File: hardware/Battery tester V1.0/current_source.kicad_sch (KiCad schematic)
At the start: 13 parts, among them K1 Relay_DPDT, Q1 IRF540N, U1 LM358

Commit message: update man pcb, cleanup
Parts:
- added C4: 100n, Capacitor_SMD:C_0805_2012Metric_Pad1.18x1.45mm_HandSolder, symbol Device:C
- added D1: 1N4148, Diode_THT:D_DO-35_SOD27_P7.62mm_Horizontal, symbol Diode:1N4148
- added Q2: BC817, Package_TO_SOT_SMD:SOT-23, symbol Transistor_BJT:BC817
- added R12: 10k, symbol Device:R
- C1: value C -> 100n; footprint (none) -> Capacitor_SMD:C_0805_2012Metric_Pad1.18x1.45mm_HandSolder
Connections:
- net GND: now reaches C3.2, R9.1
- net GND: now also C1.2, C4.2, Q2.2 (E)
- net -5V: now reaches U1.4 (V-)
- net -5V: now also C4.1
- net +5V: now reaches C1.1, U1.8 (V+)
- net +12V: now reaches K1.A1
- net +12V: now also D1.1 (K)
- net at K1.A2: now also D1.2 (A), Q2.3 (C)
- new net: Q2.1 (B), R12.1
- new net SWITCH_RANGE: R12.2

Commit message: update main pcb schematic
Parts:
- C10: renamed from C2; footprint (none) -> Capacitor_SMD:C_0805_2012Metric_Pad1.18x1.45mm_HandSolder
- C9: renamed from C3; footprint (none) -> Capacitor_SMD:C_0805_2012Metric_Pad1.18x1.45mm_HandSolder
- R10: renamed from R6; footprint (none) -> Capacitor_SMD:C_0805_2012Metric_Pad1.18x1.45mm_HandSolder
- R11: renamed from R3; footprint (none) -> Capacitor_SMD:C_0805_2012Metric_Pad1.18x1.45mm_HandSolder
- R12: renamed from R4; footprint (none) -> Capacitor_SMD:C_0805_2012Metric_Pad1.18x1.45mm_HandSolder
- R5: renamed from R8; footprint (none) -> Capacitor_SMD:C_0805_2012Metric_Pad1.18x1.45mm_HandSolder
- R6: renamed from R9; footprint (none) -> Capacitor_SMD:C_0805_2012Metric_Pad1.18x1.45mm_HandSolder
- R7: footprint (none) -> Capacitor_SMD:C_0805_2012Metric_Pad1.18x1.45mm_HandSolder
- R8: renamed from R12; footprint (none) -> Capacitor_SMD:C_0805_2012Metric_Pad1.18x1.45mm_HandSolder
- R9: renamed from R5; footprint (none) -> Capacitor_SMD:C_0805_2012Metric_Pad1.18x1.45mm_HandSolder
- U2: renamed from U1; footprint (none) -> Package_SO:SO-8_3.9x4.9mm_P1.27mm
- renumbered C1 to C7, C4 to C8, Q2 to Q1, Q1 to Q2
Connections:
- net DAC_CURRENT: now reaches U2.3 (+)
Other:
- note added: "DISCHARGE CURRENT FEEDBACK"
- note added: "DISCHARGE CURRENT RANGE SELECTOR"
- note added: "DISCHARGE CURRENT SOURCE REGULATOR"
- moved on the sheet: C10, C7, C8, C9, D1, K1, Q1, Q2, R10, R11, R12, R5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

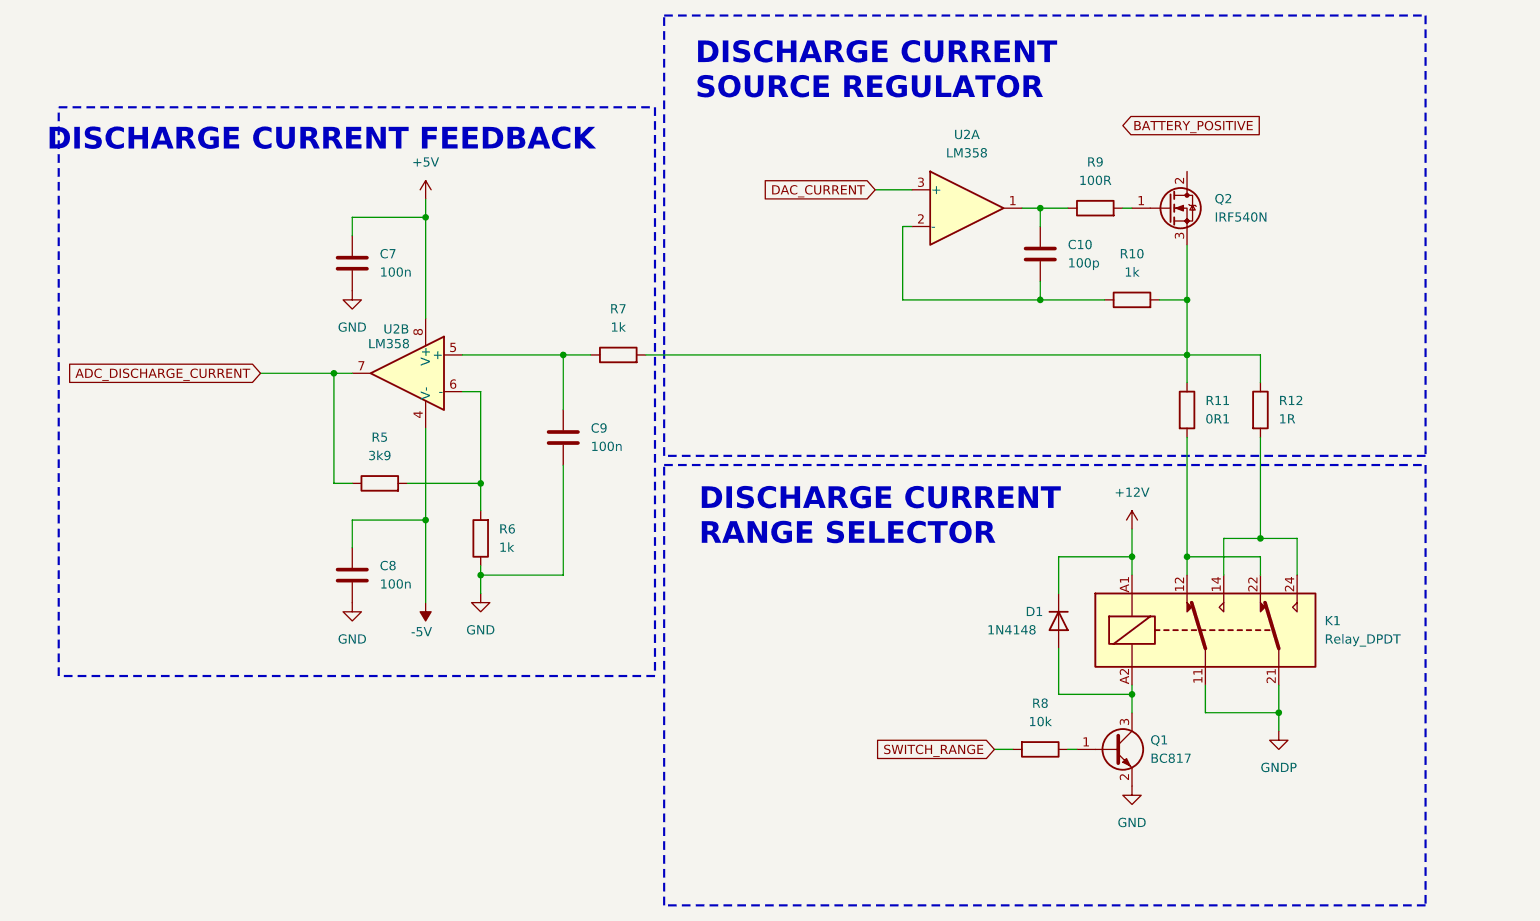
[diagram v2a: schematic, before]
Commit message: update main pcb battery charger
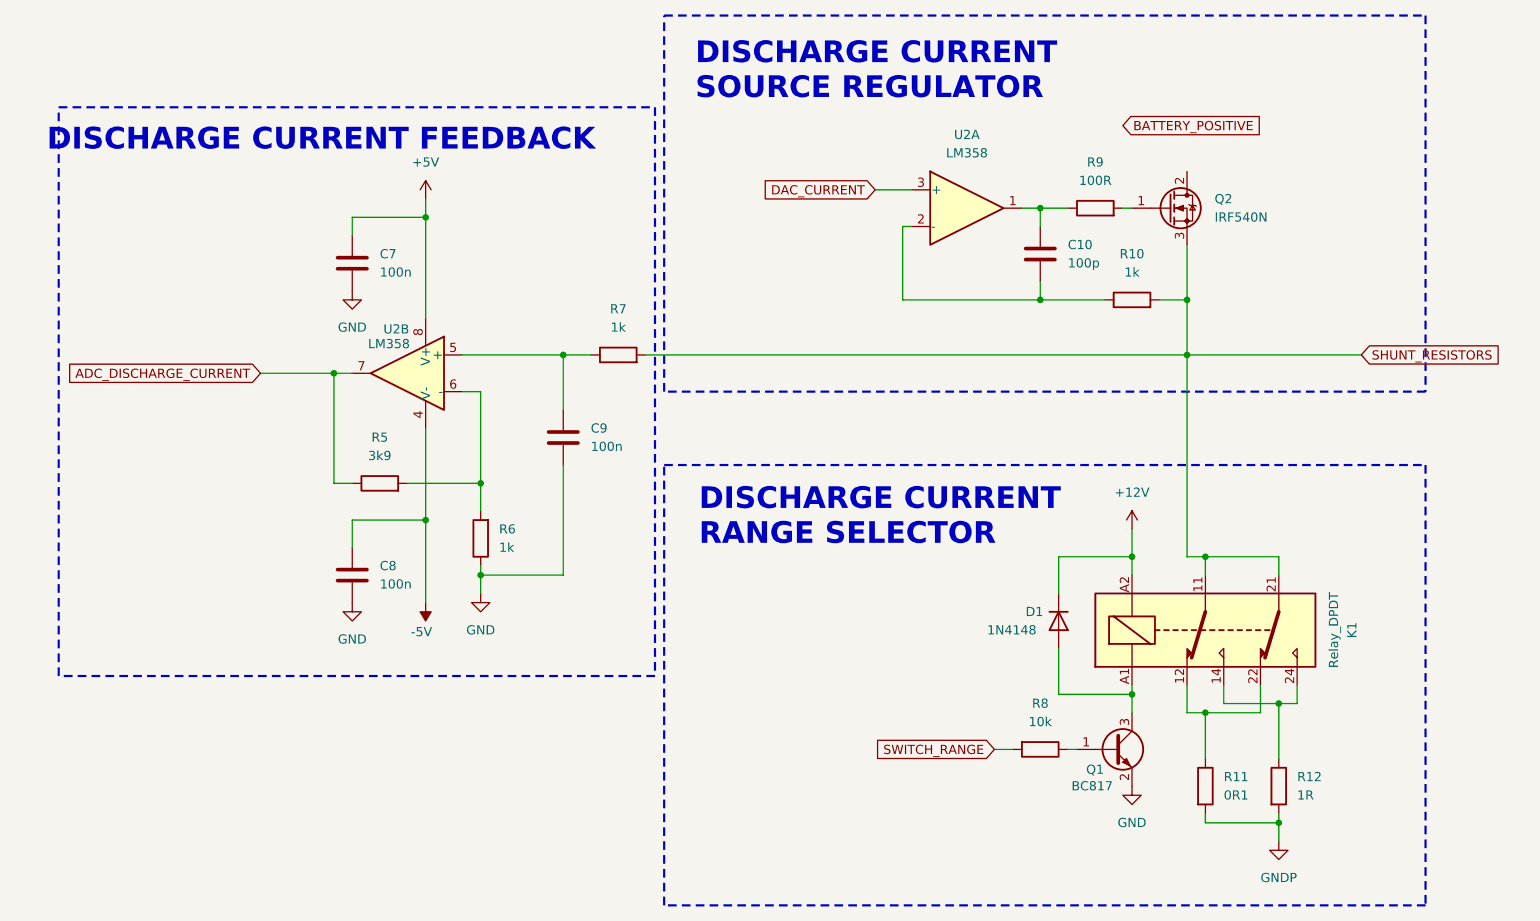
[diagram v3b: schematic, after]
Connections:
- net +12V: now also K1.A2; no longer K1.A1
- net GNDP: now also R11.2, R12.2; no longer K1.11, K1.21
- net SHUNT_RESISTORS: now reaches Q2.3 (S), R10.2, R7.2
- net SHUNT_RESISTORS: now also K1.11, K1.21; no longer R11.1, R12.1
- net at K1.12, K1.22: now also R11.1; no longer R11.2
- net at K1.14, K1.24: now also R12.1; no longer R12.2
- net at D1.2 (A), Q1.3 (C): now also K1.A1; no longer K1.A2
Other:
- moved on the sheet: R11, R12

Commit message: update schematic
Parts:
- removed C10: 100p, Capacitor_SMD:C_0805_2012Metric_Pad1.18x1.45mm_HandSolder, symbol Device:C
- removed C7, C8, C9: 100n, Capacitor_SMD:C_0805_2012Metric_Pad1.18x1.45mm_HandSolder, symbol Device:C
- removed D1: 1N4148, Diode_THT:D_DO-35_SOD27_P7.62mm_Horizontal, symbol Diode:1N4148
- removed K1: Relay_DPDT, symbol Relay:Relay_DPDT
- removed Q1: BC817, Package_TO_SOT_SMD:SOT-23, symbol Transistor_BJT:BC817
- removed Q2: IRF540N, Package_TO_SOT_THT:TO-220-3_Vertical, symbol Transistor_FET:IRF540N
- removed R10, R6, R7: 1k, Capacitor_SMD:C_0805_2012Metric_Pad1.18x1.45mm_HandSolder, symbol Device:R
- removed R11: 0R1, Capacitor_SMD:C_0805_2012Metric_Pad1.18x1.45mm_HandSolder, symbol Device:R
- removed R12: 1R, Capacitor_SMD:C_0805_2012Metric_Pad1.18x1.45mm_HandSolder, symbol Device:R
- removed R5: 3k9, Capacitor_SMD:C_0805_2012Metric_Pad1.18x1.45mm_HandSolder, symbol Device:R
- removed R8: 10k, Capacitor_SMD:C_0805_2012Metric_Pad1.18x1.45mm_HandSolder, symbol Device:R
- removed R9: 100R, Capacitor_SMD:C_0805_2012Metric_Pad1.18x1.45mm_HandSolder, symbol Device:R
- removed U2: LM358, Package_SO:SO-8_3.9x4.9mm_P1.27mm, symbol Amplifier_Operational:LM358
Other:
- note removed: "DISCHARGE CURRENT FEEDBACK"
- note removed: "DISCHARGE CURRENT RANGE SELECTOR"
- note removed: "DISCHARGE CURRENT SOURCE REGULATOR"
